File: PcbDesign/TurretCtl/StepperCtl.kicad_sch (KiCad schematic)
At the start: 10 parts

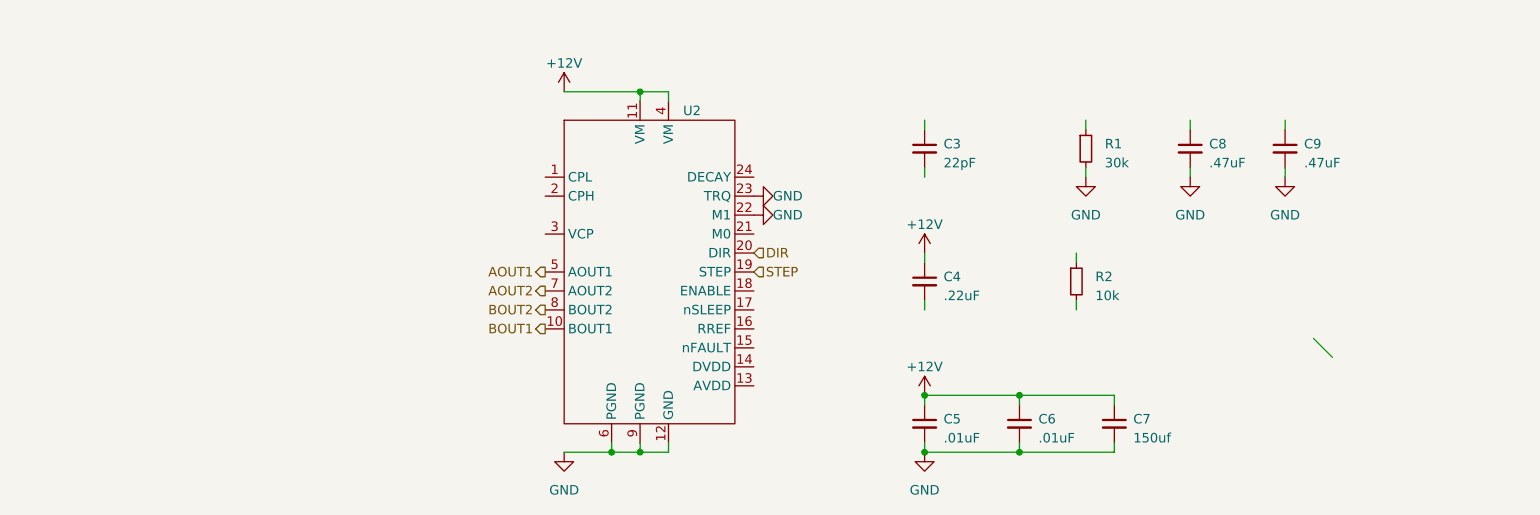
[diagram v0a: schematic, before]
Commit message: Foot print selection
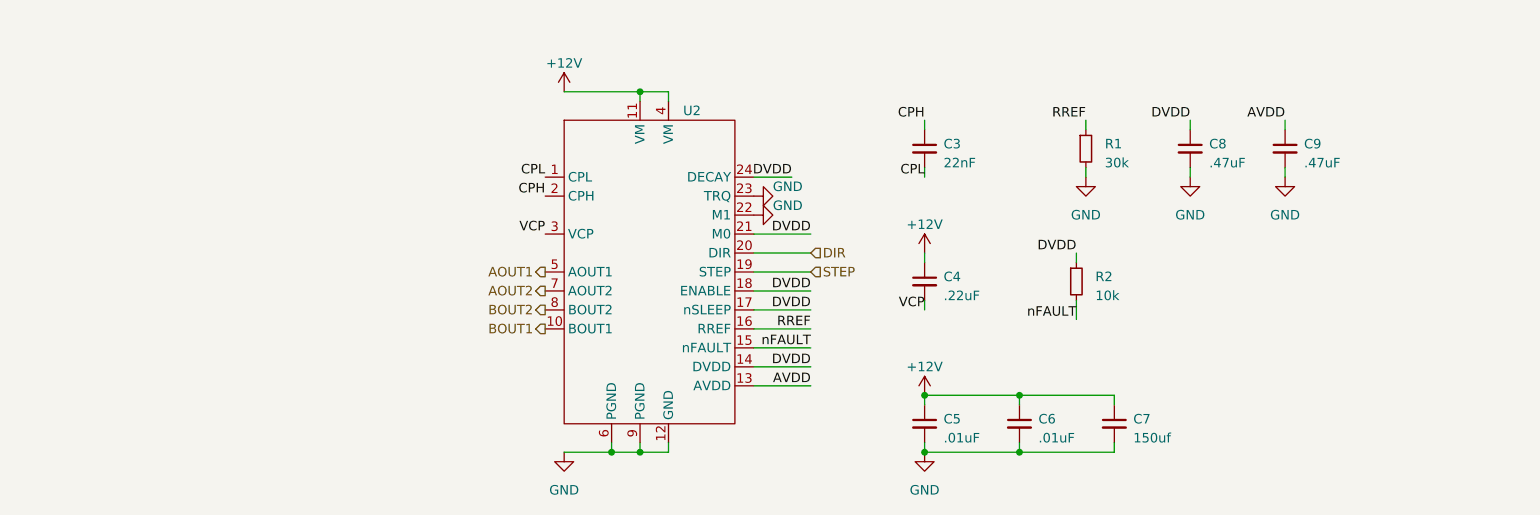
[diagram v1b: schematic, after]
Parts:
- C3: value 22pF -> 22nF; footprint (none) -> Capacitor_SMD:C_0402_1005Metric
- C4, C5, C6, C8, C9: footprint (none) -> Capacitor_SMD:C_0402_1005Metric
- C7: footprint (none) -> Capacitor_THT:C_Radial_D8.0mm_H11.5mm_P3.50mm
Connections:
- net RREF: now reaches R1.1
- net RREF: now also U2.16 (RREF)
- net CPL: now reaches U2.1 (CPL)
- net CPL: now also C3.2
- net AVDD: now reaches U2.13 (AVDD)
- net AVDD: now also C9.1
- net DVDD: now reaches U2.14 (DVDD)
- net DVDD: now also C8.1, R2.1, U2.17 (nSLEEP), U2.18 (ENABLE), U2.21 (M0), U2.24 (DECAY)
- net nFAULT: now reaches U2.15 (nFAULT)
- net nFAULT: now also R2.2
- net CPH: now reaches U2.2 (CPH)
- net CPH: now also C3.1
- net VCP: now reaches U2.3 (VCP)
- net VCP: now also C4.2

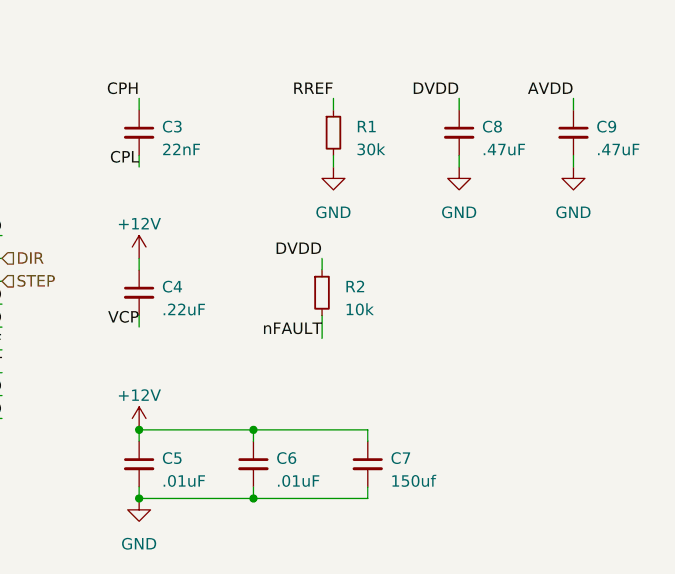
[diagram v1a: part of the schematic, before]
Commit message: Reader for JLCPCB run
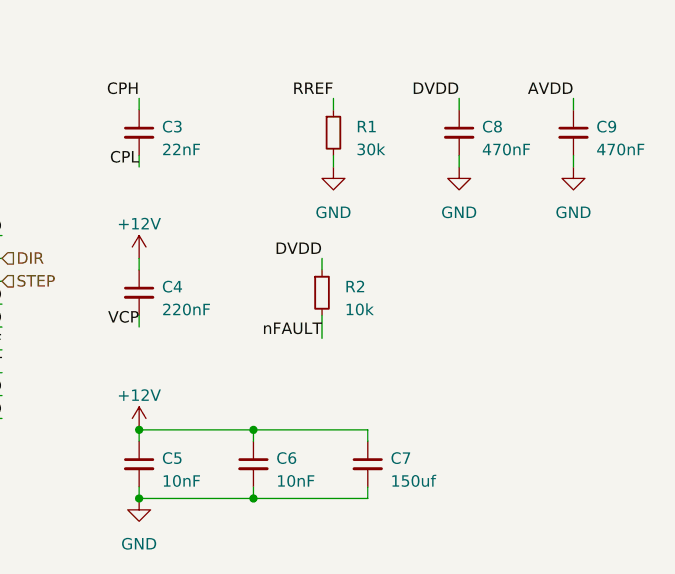
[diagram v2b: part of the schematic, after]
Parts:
- C3: LCSC Part (none) -> C1532; LCSC Part # (none) -> C1532
- C4: value .22uF -> 220nF; LCSC Part (none) -> C16772; LCSC Part # (none) -> C16772
- C5, C6: value .01uF -> 10nF; LCSC Part (none) -> C15195; LCSC Part # (none) -> C15195
- C7: footprint Capacitor_THT:C_Radial_D8.0mm_H11.5mm_P3.50mm -> Capacitor_THT:C_Radial_D10.0mm_H12.5mm_P5.00mm; LCSC Part (none) -> C432404; LCSC Part # (none) -> C432404
- C8, C9: value .47uF -> 470nF; LCSC Part (none) -> C437526; LCSC Part # (none) -> C437526
- R1: footprint (none) -> Resistor_SMD:R_0402_1005Metric; LCSC Part (none) -> C25779; LCSC Part # (none) -> C25779
- R2: footprint (none) -> Resistor_SMD:R_0402_1005Metric; LCSC Part (none) -> C25744; LCSC Part # (none) -> C25744
- U2: footprint (none) -> Package_SO:HTSSOP-24-1EP_4.4x7.8mm_P0.65mm_EP3.4x7.8mm_Mask2.4x2.98mm
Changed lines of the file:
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@@
       (effects (font (size 1.27 1.27)) (justify left))
     )
-    (property "Footprint" "" (at 198.12 68.58 0)
+    (property "Footprint" "Resistor_SMD:R_0402_1005Metric" (at 198.12 68.58 0)
       (effects (font (size 1.27 1.27)) hide)
     )
@@
       (effects (font (size 1.27 1.27)) hide)
     )
+    (property "LCSC Part #" "C25779" (at 198.12 68.58 0)
+      (effects (font (size 1.27 1.27)) hide)
+    )
+    (property "LCSC Part" "C25779" (at 198.12 68.58 0)
+      (effects (font (size 1.27 1.27)) hide)
+    )
     (pin "1")
     (pin "2")
@@
       (effects (font (size 1.27 1.27)))
     )
-    (property "Footprint" "" (at 138.43 60.96 0)
+    (property "Footprint" "Package_SO:HTSSOP-24-1EP_4.4x7.8mm_P0.65mm_EP3.4x7.8mm_Mask2.4x2.98mm" (at 138.43 60.96 0)
       (effects (font (size 1.27 1.27)) hide)
     )
     (property "Datasheet" "" (at 138.43 60.96 0)
+      (effects (font (size 1.27 1.27)) hide)
+    )
+    (property "LCSC Part #" "" (at 138.43 85.09 0)
+      (effects (font (size 1.27 1.27)) hide)
+    )
+    (property "LCSC Part" "" (at 138.43 85.09 0)
       (effects (font (size 1.27 1.27)) hide)
     )
@@
       (effects (font (size 1.27 1.27)) (justify left))
     )
-    (property "Value" ".22uF" (at 179.07 88.2713 0)
+    (property "Value" "220nF" (at 179.07 88.2713 0)
       (effects (font (size 1.27 1.27)) (justify left))
     )
@@
     )
     (property "Datasheet" "~" (at 176.53 86.36 0)
+      (effects (font (size 1.27 1.27)) hide)
+    )
+    (property "LCSC Part #" "C16772" (at 176.53 86.36 0)
+      (effects (font (size 1.27 1.27)) hide)
+    )
+    (property "LCSC Part" "C16772" (at 176.53 86.36 0)
       (effects (font (size 1.27 1.27)) hide)
     )
@@
       (effects (font (size 1.27 1.27)) (justify left))
     )
-    (property "Value" ".47uF" (at 227.33 70.4913 0)
+    (property "Value" "470nF" (at 227.33 70.4913 0)
       (effects (font (size 1.27 1.27)) (justify left))
     )
@@
       (effects (font (size 1.27 1.27)) hide)
     )
+    (property "LCSC Part #" "C437526" (at 224.79 68.58 0)
+      (effects (font (size 1.27 1.27)) hide)
+    )
+    (property "LCSC Part" "C437526" (at 224.79 68.58 0)
+      (effects (font (size 1.27 1.27)) hide)
+    )
     (pin "1")
     (pin "2")
@@
       (effects (font (size 1.27 1.27)) hide)
     )
+    (property "LCSC Part #" "C1532" (at 176.53 68.58 0)
+      (effects (font (size 1.27 1.27)) hide)
+    )
+    (property "LCSC Part" "C1532" (at 176.53 68.58 0)
+      (effects (font (size 1.27 1.27)) hide)
+    )
     (pin "1")
     (pin "2")
@@
       (effects (font (size 1.27 1.27)) (justify left))
     )
-    (property "Value" ".01uF" (at 191.77 107.3213 0)
+    (property "Value" "10nF" (at 191.77 107.3213 0)
       (effects (font (size 1.27 1.27)) (justify left))
     )
@@
       (effects (font (size 1.27 1.27)) hide)
     )
+    (property "LCSC Part #" "C15195" (at 189.23 105.41 0)
+      (effects (font (size 1.27 1.27)) hide)
+    )
+    (property "LCSC Part" "C15195" (at 189.23 105.41 0)
+      (effects (font (size 1.27 1.27)) hide)
+    )
     (pin "1")
     (pin "2")
@@
       (effects (font (size 1.27 1.27)) (justify left))
     )
-    (property "Footprint" "" (at 196.85 86.36 0)
+    (property "Footprint" "Resistor_SMD:R_0402_1005Metric" (at 196.85 86.36 0)
       (effects (font (size 1.27 1.27)) hide)
     )
@@
       (effects (font (size 1.27 1.27)) hide)
     )
+    (property "LCSC Part #" "C25744" (at 196.85 86.36 0)
+      (effects (font (size 1.27 1.27)) hide)
+    )
+    (property "LCSC Part" "C25744" (at 196.85 86.36 0)
+      (effects (font (size 1.27 1.27)) hide)
+    )
     (pin "1")
     (pin "2")
@@
       (effects (font (size 1.27 1.27)) (justify left))
     )
-    (property "Value" ".01uF" (at 179.07 107.3213 0)
+    (property "Value" "10nF" (at 179.07 107.3213 0)
       (effects (font (size 1.27 1.27)) (justify left))
     )
@@
       (effects (font (size 1.27 1.27)) hide)
     )
+    (property "LCSC Part #" "C15195" (at 176.53 105.41 0)
+      (effects (font (size 1.27 1.27)) hide)
+    )
+    (property "LCSC Part" "C15195" (at 176.53 105.41 0)
+      (effects (font (size 1.27 1.27)) hide)
+    )
     (pin "1")
     (pin "2")
@@
       (effects (font (size 1.27 1.27)) (justify left))
     )
-    (property "Value" ".47uF" (at 214.63 70.4913 0)
+    (property "Value" "470nF" (at 214.63 70.4913 0)
       (effects (font (size 1.27 1.27)) (justify left))
     )
@@
       (effects (font (size 1.27 1.27)) hide)
     )
+    (property "LCSC Part #" "C437526" (at 212.09 68.58 0)
+      (effects (font (size 1.27 1.27)) hide)
+    )
+    (property "LCSC Part" "C437526" (at 212.09 68.58 0)
+      (effects (font (size 1.27 1.27)) hide)
+    )
     (pin "1")
     (pin "2")
@@
       (effects (font (size 1.27 1.27)) (justify left))
     )
-    (property "Footprint" "Capacitor_THT:C_Radial_D8.0mm_H11.5mm_P3.50mm" (at 201.93 105.41 0)
+    (property "Footprint" "Capacitor_THT:C_Radial_D10.0mm_H12.5mm_P5.00mm" (at 201.93 105.41 0)
       (effects (font (size 1.27 1.27)) hide)
     )
@@
       (effects (font (size 1.27 1.27)) hide)
     )
+    (property "LCSC Part #" "C432404" (at 201.93 105.41 0)
+      (effects (font (size 1.27 1.27)) hide)
+    )
+    (property "LCSC Part" "C432404" (at 201.93 105.41 0)
+      (effects (font (size 1.27 1.27)) hide)
+    )

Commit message: Stepper Control Board V2
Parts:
- added D1 (x7): LED, LED_SMD:LED_0603_1608Metric, symbol Device:LED
- added R5 (x7): 330, Resistor_SMD:R_0402_1005Metric, symbol Device:R_Small
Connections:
- net AOUT1: now also D1.2 (A)
- net AOUT2: now also D1.2 (A)
- net BOUT1: now also D1.2 (A)
- net BOUT2: now also D1.2 (A)
- net DVDD: now also D1.2 (A); no longer U2.17 (nSLEEP), U2.18 (ENABLE)
- net GND: now also R5.2, R5.2, R5.2, R5.2, R5.2, R5.2, R5.2
- new net: D1.1 (K), R5.1 (x7)
- new net +5V: D1.2 (A), D1.2 (A), U2.17 (nSLEEP), U2.18 (ENABLE)
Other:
- moved on the sheet: C9, U2

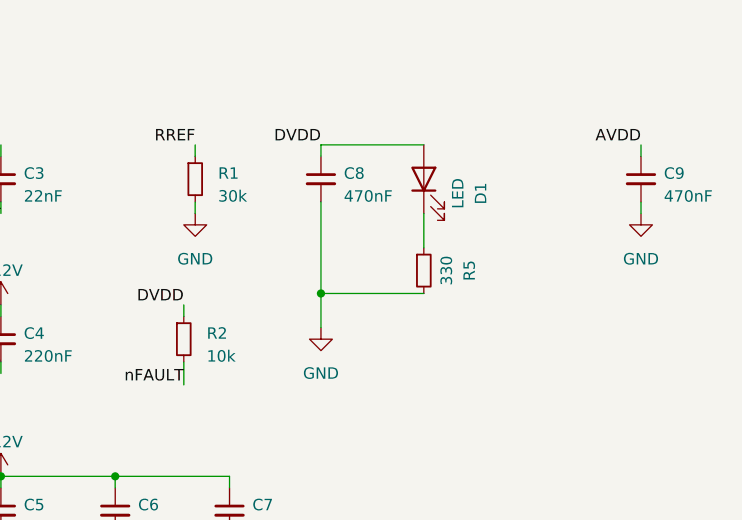
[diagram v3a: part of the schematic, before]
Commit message: Removed dvdd leds
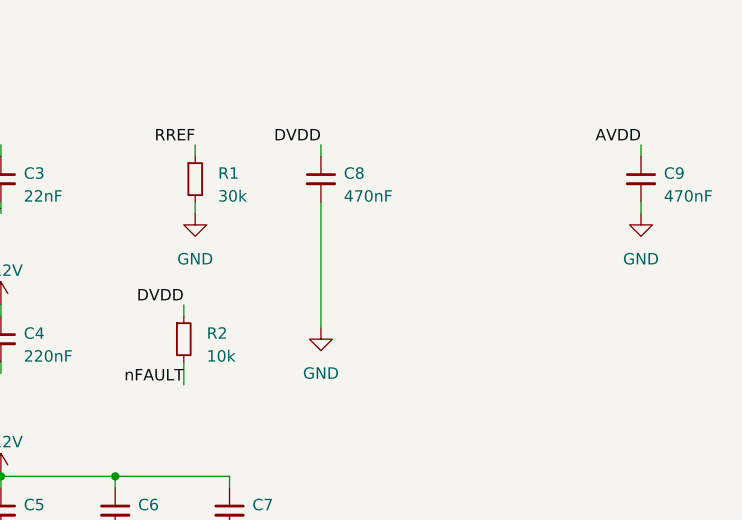
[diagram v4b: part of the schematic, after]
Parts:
- removed D1: LED, LED_SMD:LED_0603_1608Metric, symbol Device:LED
- removed R5: 330, Resistor_SMD:R_0402_1005Metric, symbol Device:R_Small
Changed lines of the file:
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@@
   (junction (at 176.53 101.6) (diameter 0) (color 0 0 0 0)
   )
-  (junction (at 212.09 81.28) (diameter 0) (color 0 0 0 0)
-  )
   (junction (at 93.98 85.09) (diameter 0) (color 0 0 0 0)
   )
@@
   (junction (at 161.29 87.63) (diameter 0) (color 0 0 0 0)
   )
-  (wire (pts (xy 212.09 71.12) (xy 212.09 81.28))
+  (wire (pts (xy 212.09 71.12) (xy 212.09 85.09))
     (stroke (width 0) (type default))
   )
@@
     (stroke (width 0) (type default))
   )
-  (wire (pts (xy 212.09 64.77) (xy 223.52 64.77))
-    (stroke (width 0) (type default))
-  )
   (wire (pts (xy 247.65 71.12) (xy 247.65 72.39))
     (stroke (width 0) (type default))
@@
     (stroke (width 0) (type default))
   )
-  (wire (pts (xy 212.09 81.28) (xy 223.52 81.28))
-    (stroke (width 0) (type default))
-  )
   (wire (pts (xy 134.62 85.09) (xy 127 85.09))
     (stroke (width 0) (type default))
@@
     (stroke (width 0) (type default))
   )
-  (wire (pts (xy 212.09 81.28) (xy 212.09 85.09))
-    (stroke (width 0) (type default))
-  )
   (wire (pts (xy 212.09 64.77) (xy 212.09 66.04))
     (stroke (width 0) (type default))
@@
   )
   (wire (pts (xy 176.53 107.95) (xy 176.53 109.22))
-    (stroke (width 0) (type default))
-  )
-  (wire (pts (xy 223.52 72.39) (xy 223.52 76.2))
     (stroke (width 0) (type default))
   )
@@
     )
   )
-  (symbol (lib_id "Device:R_Small") (at 223.52 78.74 0) (unit 1)
-    (in_bom yes) (on_board yes) (dnp no) (fields_autoplaced)
-    (property "Reference" "R5" (at 228.6 78.74 90)
-      (effects (font (size 1.27 1.27)))
-    )
-    (property "Value" "330" (at 226.06 78.74 90)
-      (effects (font (size 1.27 1.27)))
-    )
-    (property "Footprint" "Resistor_SMD:R_0402_1005Metric" (at 223.52 78.74 0)
-      (effects (font (size 1.27 1.27)) hide)
-    )
-    (property "Datasheet" "~" (at 223.52 78.74 0)
-      (effects (font (size 1.27 1.27)) hide)
-    )
-    (property "LCSC Part #" "C25104" (at 223.52 78.74 0)
-      (effects (font (size 1.27 1.27)) hide)
-    )
-    (property "LCSC Part" "C25104" (at 223.52 78.74 0)
-      (effects (font (size 1.27 1.27)) hide)
-    )
-    (pin "1")
-    (pin "2")
-    (instances
-      (project "TurretCtl"
-        (path "/2b45bb67-e901-4104-9ea3-7ba76f788dce"
-          (reference "R5") (unit 1)
-        )
-        (path "/2b45bb67-e901-4104-9ea3-7ba76f788dce/9d77d4b7-dc15-471e-94c5-254ad55bf7a4"
-          (reference "R14") (unit 1)
-        )
-        (path "/2b45bb67-e901-4104-9ea3-7ba76f788dce/a9029235-dc0e-47ba-826b-288be698a9f2"
-          (reference "R15") (unit 1)
-        )
-      )
-    )
-  )
   (symbol (lib_id "power:GND") (at 127 77.47 90) (unit 1)
     (in_bom yes) (on_board yes) (dnp no)
@@
         )
       )
-    )
-  )
-  (symbol (lib_id "Device:LED") (at 223.52 68.58 90) (unit 1)
-    (in_bom yes) (on_board yes) (dnp no) (fields_autoplaced)
-    (property "Reference" "D1" (at 229.87 70.1675 0)
-      (effects (font (size 1.27 1.27)))
-    )
-    (property "Value" "LED" (at 227.33 70.1675 0)
-      (effects (font (size 1.27 1.27)))
-    )
-    (property "Footprint" "LED_SMD:LED_0603_1608Metric" (at 223.52 68.58 0)
-      (effects (font (size 1.27 1.27)) hide)
-    )
-    (property "Datasheet" "~" (at 223.52 68.58 0)
-      (effects (font (size 1.27 1.27)) hide)
-    )
-    (property "LCSC Part #" "C2286" (at 223.52 68.58 0)
-      (effects (font (size 1.27 1.27)) hide)
-    )
-    (property "LCSC Part" "C2286" (at 223.52 68.58 0)
-      (effects (font (size 1.27 1.27)) hide)
-    )
-    (pin "1")
-    (pin "2")
-    (instances
-      (project "TurretCtl"
-        (path "/2b45bb67-e901-4104-9ea3-7ba76f788dce"
-          (reference "D1") (unit 1)
-        )
-        (path "/2b45bb67-e901-4104-9ea3-7ba76f788dce/9d77d4b7-dc15-471e-94c5-254ad55bf7a4"
-          (reference "D10") (unit 1)
-        )
-        (path "/2b45bb67-e901-4104-9ea3-7ba76f788dce/a9029235-dc0e-47ba-826b-288be698a9f2"
-          (reference "D11") (unit 1)
-        )
-      )
